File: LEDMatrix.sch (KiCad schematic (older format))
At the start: 79 parts

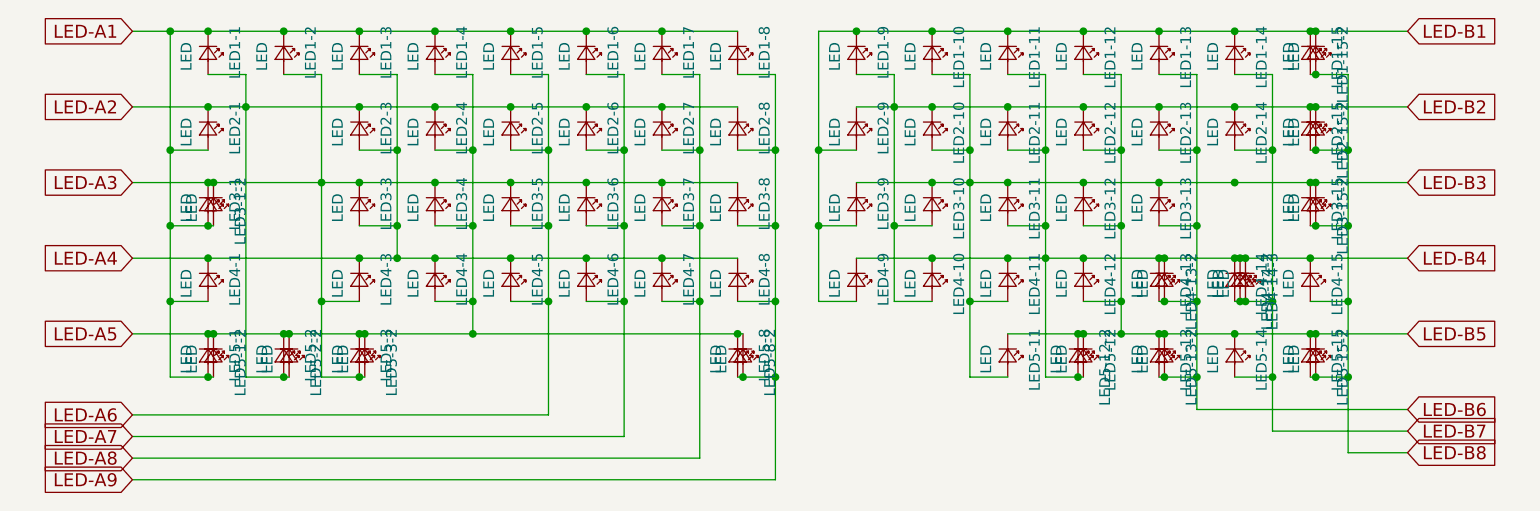
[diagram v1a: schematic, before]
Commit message: Add LEDs
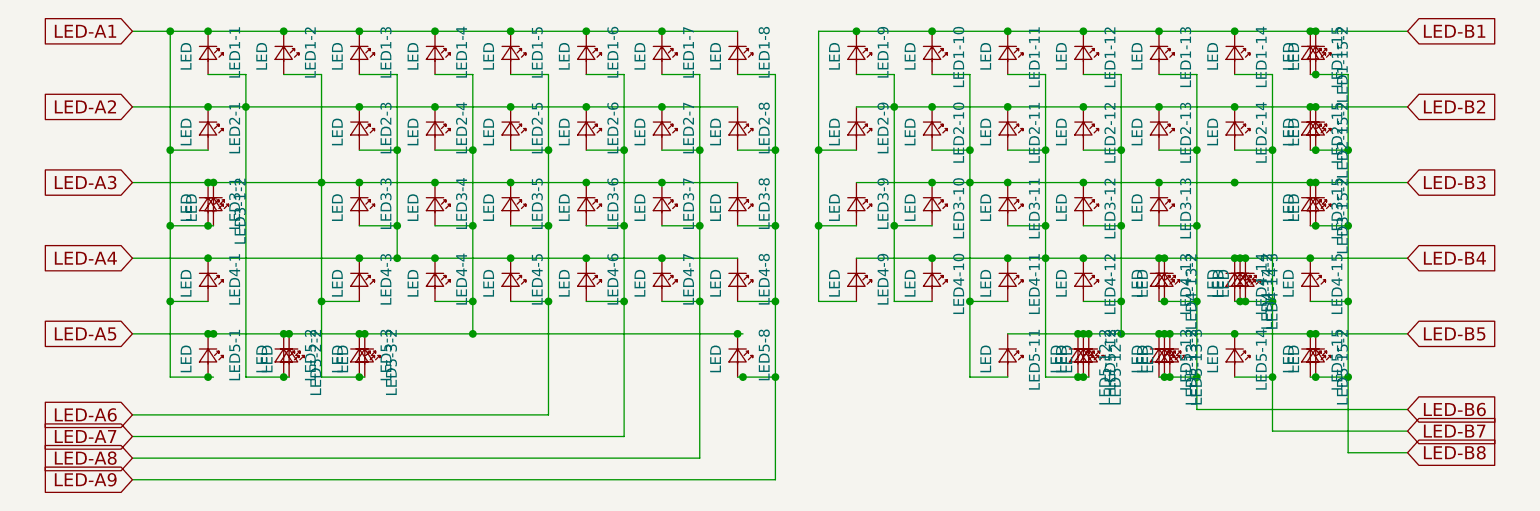
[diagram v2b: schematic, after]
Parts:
- removed LED5-1-2: LED, MX_Alps_Hybrid:LED-FLIPPED, symbol LED_Small
- removed LED5-8-2: LED, MX_Alps_Hybrid:LED, symbol LED_Small
- added LED5-12-3: LED, MX_Alps_Hybrid:LED-FLIPPED, symbol LED_Small
- added LED5-13-3: LED, MX_Alps_Hybrid:LED, symbol LED_Small
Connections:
- net LED-B4: now also LED5-12-3.2 (A)
- net LED-B5: now also LED5-12-3.1 (K), LED5-13-3.1 (K)
- net LED-B6: now also LED5-13-3.2 (A)
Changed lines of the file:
@@
 Connection ~ 6075 2400
 Wire Wire Line
-	6075 3450 6250 3450
+	6075 3450 6275 3450
 Wire Wire Line
 	6250 2050 6425 2050
@@
 	7475 3800 7750 3800
 Connection ~ 7475 3450
-$Comp
-L LED_Small LED5-1-2
-U 1 1 5A6D85C3
-P 2225 3350
-F 0 "LED5-1-2" H 2100 3475 50  0000 L CNN
-F 1 "LED" H 2175 3250 50  0000 L CNN
-F 2 "MX_Alps_Hybrid:LED-FLIPPED" V 2225 3350 50  0001 C CNN
-F 3 "" V 2225 3350 50  0001 C CNN
-	1    2225 3350
-	0    1    1    0
-$EndComp
 $Comp
 L LED_Small LED5-2-2
@@
 Connection ~ 2900 3450
 Connection ~ 2925 3250
-$Comp
-L LED_Small LED5-8-2
-U 1 1 5A6DC14A
-P 4675 3350
-F 0 "LED5-8-2" H 4550 3475 50  0000 L CNN
-F 1 "LED" H 4625 3250 50  0000 L CNN
-F 2 "MX_Alps_Hybrid:LED" V 4675 3350 50  0001 C CNN
-F 3 "" V 4675 3350 50  0001 C CNN
-	1    4675 3350
-	0    1    1    0
-$EndComp
 Connection ~ 4650 3250
 Connection ~ 4675 3450
@@
 Connection ~ 7325 3450
 Connection ~ 7325 3250
+$Comp
+L LED_Small LED5-12-3
+U 1 1 5A78D637
+P 6275 3350
+F 0 "LED5-12-3" H 6150 3475 50  0000 L CNN
+F 1 "LED" H 6225 3250 50  0000 L CNN
+F 2 "MX_Alps_Hybrid:LED-FLIPPED" V 6275 3350 50  0001 C CNN
+F 3 "" V 6275 3350 50  0001 C CNN
+	1    6275 3350
+	0    1    1    0
+$EndComp
+Connection ~ 6250 3450
+Connection ~ 6275 3250
+$Comp
+L LED_Small LED5-13-3
+U 1 1 5A78D96A
+P 6650 3350
+F 0 "LED5-13-3" H 6525 3475 50  0000 L CNN
+F 1 "LED" H 6600 3250 50  0000 L CNN
+F 2 "MX_Alps_Hybrid:LED" V 6650 3350 50  0001 C CNN
+F 3 "" V 6650 3350 50  0001 C CNN
+	1    6650 3350
+	0    1    1    0
+$EndComp
+Connection ~ 6650 3250
+Connection ~ 6650 3450
 $EndSCHEMATC

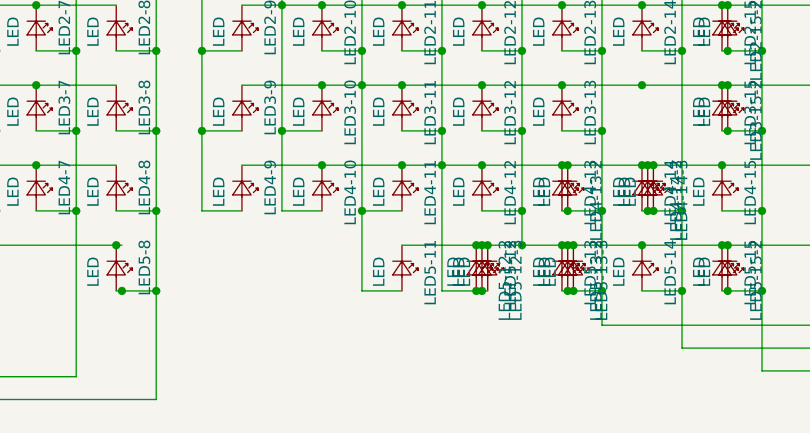
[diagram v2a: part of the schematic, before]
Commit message: Place LEDs and move out diodes
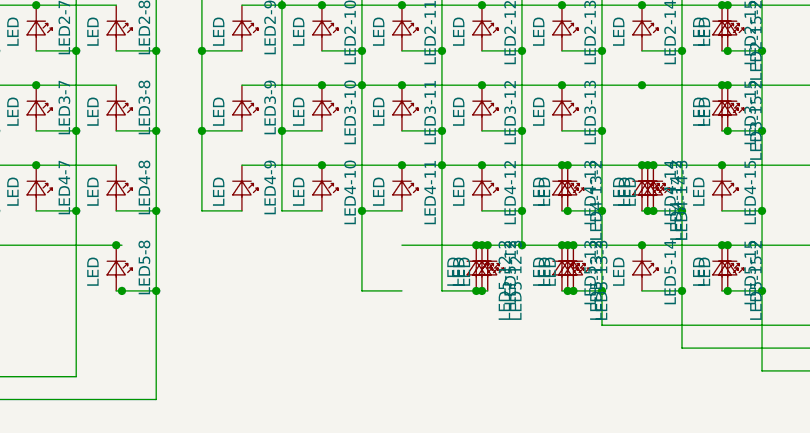
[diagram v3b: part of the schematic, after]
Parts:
- removed LED5-11: LED, MX_Alps_Hybrid:LED, symbol LED_Small
- LED5-12-3: footprint MX_Alps_Hybrid:LED-FLIPPED -> MX_Alps_Hybrid:LED
- LED5-13-3: footprint MX_Alps_Hybrid:LED -> MX_Alps_Hybrid:LED-FLIPPED
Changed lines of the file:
@@
-$EndComp
-$Comp
-L LED_Small LED5-11
-U 1 1 5A6E144D
-P 5900 3350
-F 0 "LED5-11" H 5775 3475 50  0000 L CNN
-F 1 "LED" H 5850 3250 50  0000 L CNN
-F 2 "MX_Alps_Hybrid:LED" V 5900 3350 50  0001 C CNN
-F 3 "" V 5900 3350 50  0001 C CNN
-	1    5900 3350
-	0    1    1    0
 $EndComp
 $Comp
@@
 F 0 "LED5-12-3" H 6150 3475 50  0000 L CNN
 F 1 "LED" H 6225 3250 50  0000 L CNN
-F 2 "MX_Alps_Hybrid:LED-FLIPPED" V 6275 3350 50  0001 C CNN
+F 2 "MX_Alps_Hybrid:LED" V 6275 3350 50  0001 C CNN
 F 3 "" V 6275 3350 50  0001 C CNN
 	1    6275 3350
@@
 F 0 "LED5-13-3" H 6525 3475 50  0000 L CNN
 F 1 "LED" H 6600 3250 50  0000 L CNN
-F 2 "MX_Alps_Hybrid:LED" V 6650 3350 50  0001 C CNN
+F 2 "MX_Alps_Hybrid:LED-FLIPPED" V 6650 3350 50  0001 C CNN
 F 3 "" V 6650 3350 50  0001 C CNN
 	1    6650 3350

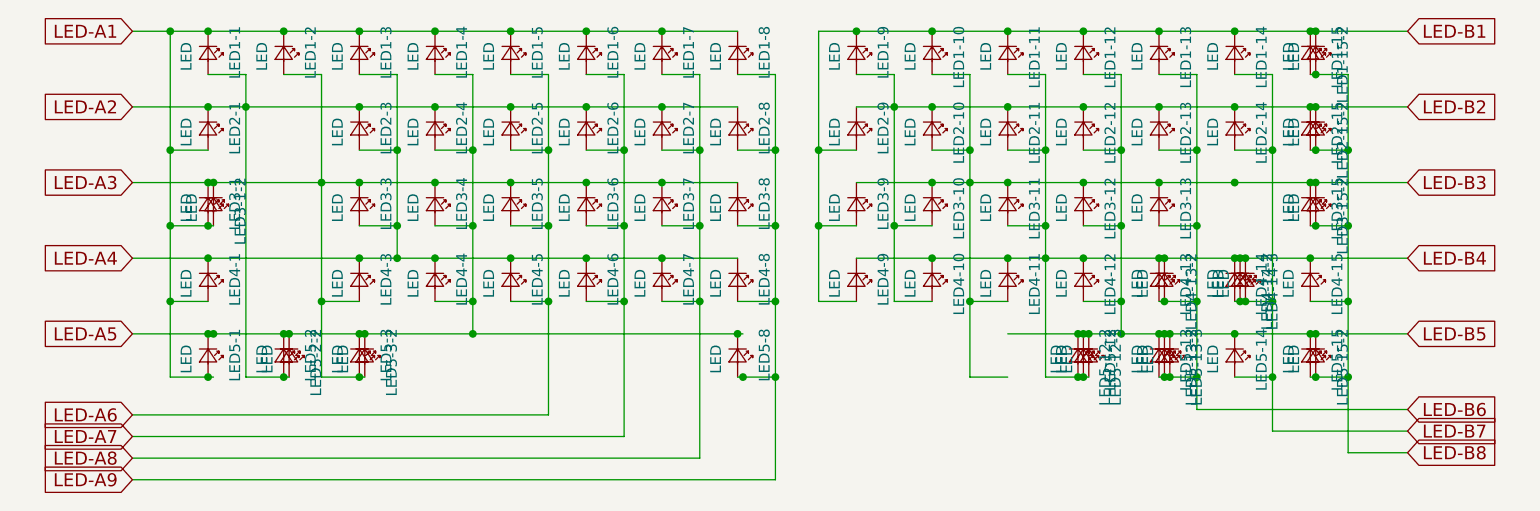
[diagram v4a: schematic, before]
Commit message: Remove LEDs for removed switches on schematic
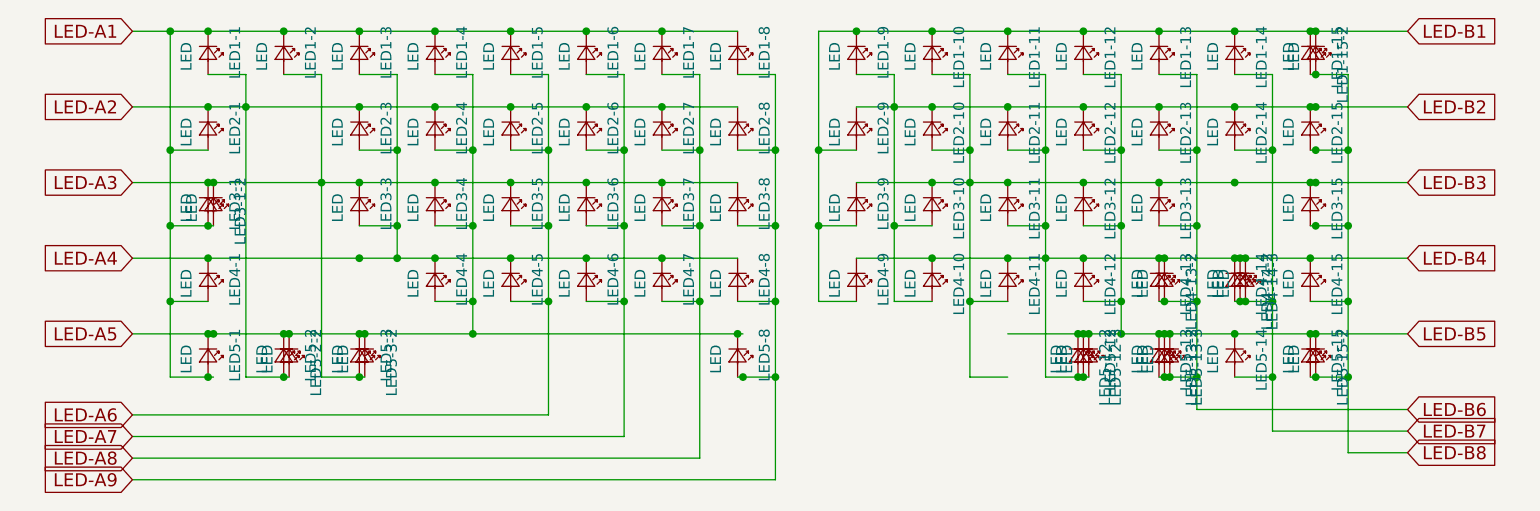
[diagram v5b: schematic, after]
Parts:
- removed LED2-15-2, LED3-15-2, LED4-3: LED, MX_Alps_Hybrid:LED, symbol LED_Small
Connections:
- wire segments 99 -> 98
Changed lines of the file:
@@
-$EndComp
-$Comp
-L LED_Small LED4-3
-U 1 1 5A6DF632
-P 2900 3000
-F 0 "LED4-3" H 2775 3125 50  0000 L CNN
-F 1 "LED" H 2850 2900 50  0000 L CNN
-F 2 "MX_Alps_Hybrid:LED" V 2900 3000 50  0001 C CNN
-F 3 "" V 2900 3000 50  0001 C CNN
-	1    2900 3000
-	0    1    1    0
 $EndComp
 $Comp
@@
 Connection ~ 2725 2550
 Wire Wire Line
-	2725 3100 2900 3100
-Wire Wire Line
 	2725 3450 2925 3450
-Connection ~ 2725 3100
 Wire Wire Line
 	3075 2050 3075 2900
@@
 Connection ~ 7325 1850
 Connection ~ 7325 2050
-$Comp
-L LED_Small LED2-15-2
-U 1 1 5A6DCCEC
-P 7325 2300
-F 0 "LED2-15-2" H 7200 2425 50  0000 L CNN
-F 1 "LED" H 7275 2200 50  0000 L CNN
-F 2 "MX_Alps_Hybrid:LED" V 7325 2300 50  0001 C CNN
-F 3 "" V 7325 2300 50  0001 C CNN
-	1    7325 2300
-	0    1    1    0
-$EndComp
 Connection ~ 7325 2200
 Connection ~ 7325 2400
-$Comp
-L LED_Small LED3-15-2
-U 1 1 5A6DD788
-P 7325 2650
-F 0 "LED3-15-2" H 7200 2775 50  0000 L CNN
-F 1 "LED" H 7275 2550 50  0000 L CNN
-F 2 "MX_Alps_Hybrid:LED" V 7325 2650 50  0001 C CNN
-F 3 "" V 7325 2650 50  0001 C CNN
-	1    7325 2650
-	0    1    1    0
-$EndComp
 Connection ~ 7325 2550
 Connection ~ 7325 2750

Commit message: Revert LED structure
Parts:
- removed LED1-1, LED1-10, LED1-11, LED1-12, LED1-13, LED1-14, LED1-15, LED1-15-2, LED1-2, LED1-3, LED1-4, LED1-5, LED1-6, LED1-7, LED1-8, LED1-9, LED2-1, LED2-10, LED2-11, LED2-12, LED2-13, LED2-14, LED2-15, LED2-3, LED2-4, LED2-5, LED2-6, LED2-7, LED2-8, LED2-9, LED3-1, LED3-10, LED3-11, LED3-12, LED3-13, LED3-15, LED3-3, LED3-4, LED3-5, LED3-6, LED3-7, LED3-8, LED3-9, LED4-1, LED4-10, LED4-11, LED4-12, LED4-13, LED4-13-2, LED4-14, LED4-14-2, LED4-15, LED4-4, LED4-5, LED4-6, LED4-7, LED4-8, LED4-9, LED5-1, LED5-12, LED5-12-3, LED5-13, LED5-13-2, LED5-14, LED5-15, LED5-2, LED5-3, LED5-8: LED, MX_Alps_Hybrid:LED, symbol LED_Small
- removed LED3-1-2, LED4-14-3, LED5-12-2, LED5-13-3, LED5-15-2, LED5-2-2, LED5-3-2: LED, MX_Alps_Hybrid:LED-FLIPPED, symbol LED_Small
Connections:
- net labels removed: LED-A1, LED-A2, LED-A3, LED-A4, LED-A5, LED-A6, LED-A7, LED-A8, LED-A9, LED-B1, LED-B2, LED-B3, LED-B4, LED-B5, LED-B6, LED-B7, LED-B8
- wire segments 98 -> 0
